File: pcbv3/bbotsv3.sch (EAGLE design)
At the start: 24 parts

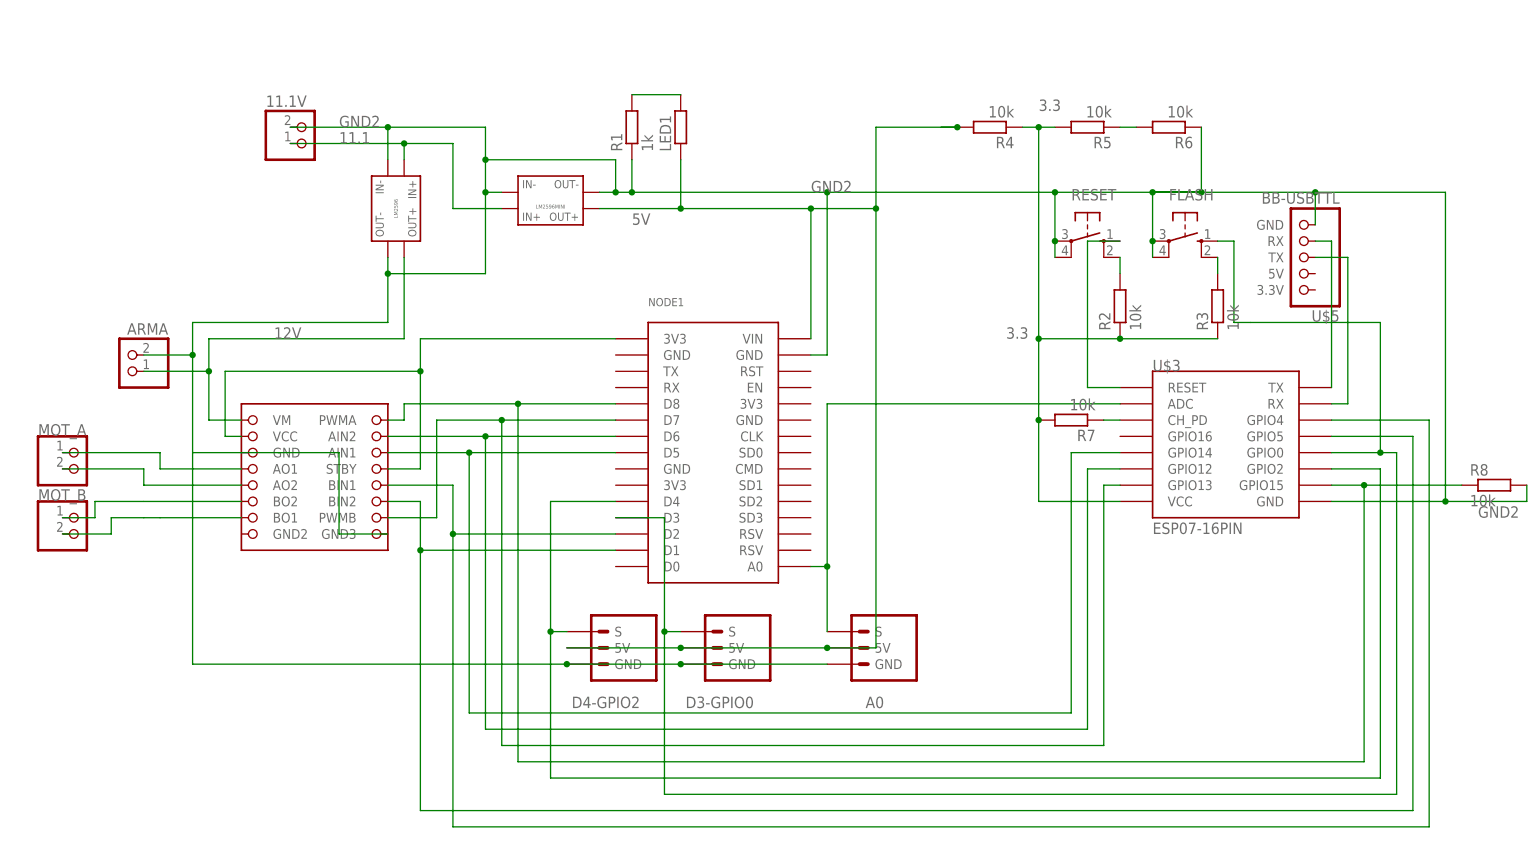
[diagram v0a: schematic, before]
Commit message: changed version of lm2596mini
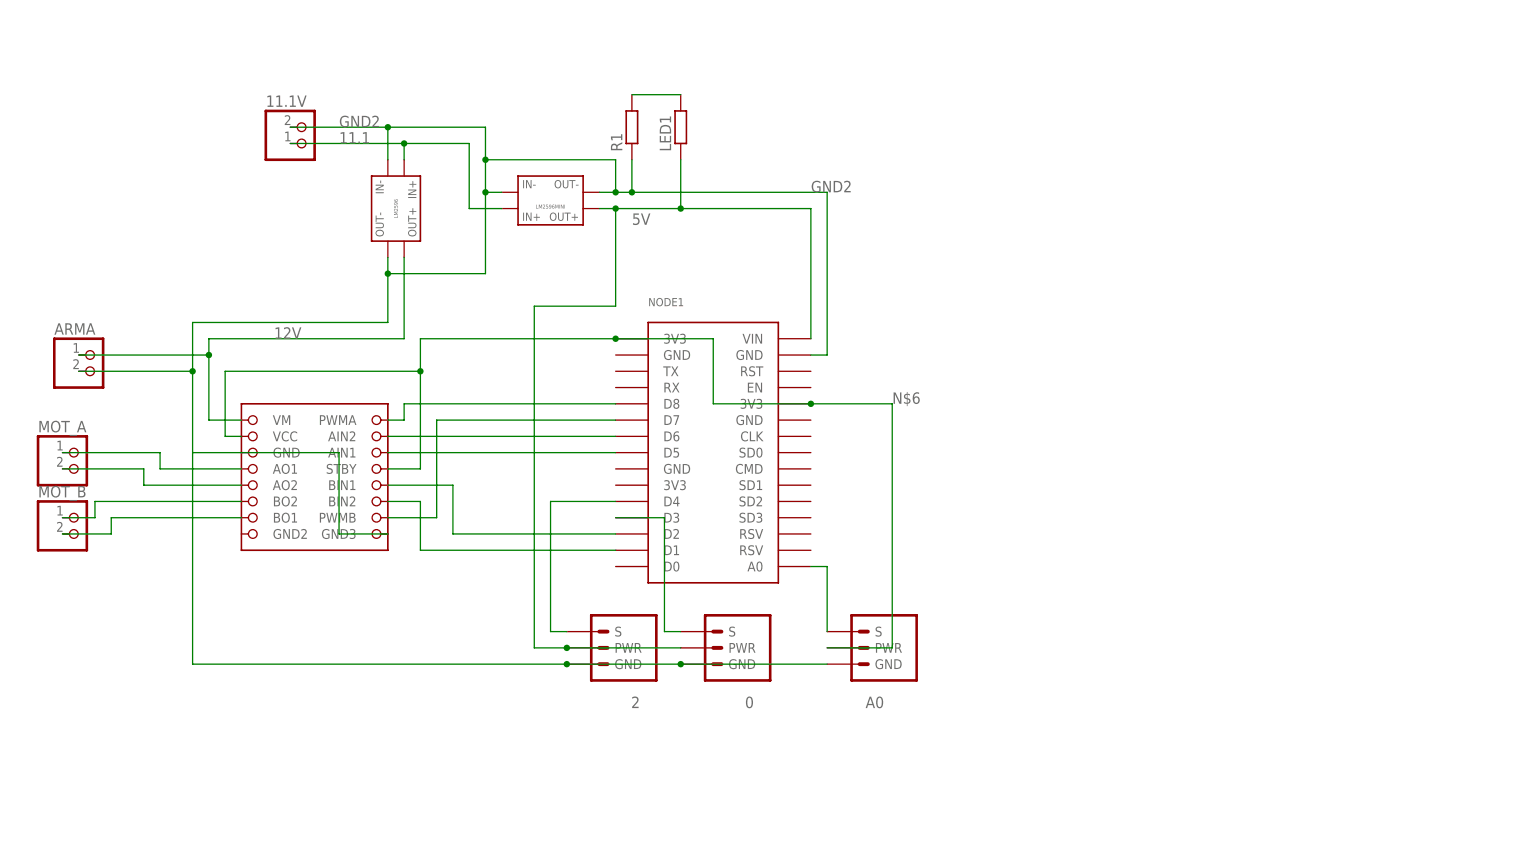
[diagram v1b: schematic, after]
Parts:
- removed D3-GPIO0, D4-GPIO2: BB-PIN3, my-library:BB-PIN3
- removed FLASH, RESET: (no value), switch-omron:10-XX
- removed R2, R3, R4, R5, R6, R7, R8: 10k, my-library:BB-RESM0805
- removed U$4: BB-LM2596MINI, my-library:BB-LM2596MINI
- removed U$5: BB-USBTTL, my-library:BB-USBTTL
- added 0, 2: BB-PIN3BB-PIN3, my-library:BB-PIN3BB-PIN3
- A0: value BB-PIN3 -> 3.3; device my-library:BB-PIN3 -> my-library:BB-PIN3BB-PIN3
- ARMA, MOT_A, MOT_B: device adafruit:JST_2PIN-THM -> my-library:JST_2PIN
- LED1: device my-library:BB-RESM0805 -> my-library:BB-R0805
- R1: value 1k -> BB-R1205; device my-library:BB-RESM0805 -> my-library:BB-R1205
- U$3: value ESP07-16PIN -> BB-LM2596MINILM2596MINIV2; device esp8266modules:ESP07-16PIN -> my-library:BB-LM2596MINILM2596MINIV2
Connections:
- removed net 3.3: R2.1, R3.1, R4.1, R5.2, R7.2, U$3.VCC
- removed net N$17: NODE1.3V3@1, U$2.STBY, U$2.VCC
- removed net N$19: U$3.TX, U$5.RX
- removed net N$20: U$3.RX, U$5.TX
- removed net N$22: R2.2, RESET.S1
- removed net N$23: FLASH.S1, R3.2
- removed net N$25: R5.1, R6.2
- removed net N$27: RESET.S, U$3.RESET
- removed net N$28: R7.1, U$3.CH_PD
- new net N$6: A0.PWR, NODE1.3V3@1, NODE1.3V3@3, U$2.STBY, U$2.VCC
- net 11.1: now also U$3.IN+; no longer U$4.IN+
- net 12V: now also ARMA.1; no longer ARMA.2
- net 5V: now also 0.PWR, 2.PWR, U$3.OUT+; no longer A0.5V, D3-GPIO0.5V, D4-GPIO2.5V, R4.2, U$4.OUT+
- net GND2: now also 0.GND, 2.GND, ARMA.2, U$3.IN-, U$3.OUT-; no longer ARMA.1, D3-GPIO0.GND, D4-GPIO2.GND, FLASH.P, FLASH.P1, R6.1, R8.2, RESET.P, RESET.P1, U$3.GND, U$4.IN-, U$4.OUT-, U$5.GND
- net N$10: no longer U$3.GPIO5
- net N$12: now also 2.S; no longer D4-GPIO2.S, U$3.GPIO2
- net N$13: now also MOT_A.2; no longer MOT_A.1
- net N$14: now also MOT_A.1; no longer MOT_A.2
- net N$15: now also MOT_B.1; no longer MOT_B.2
- net N$16: now also MOT_B.2; no longer MOT_B.1
- net N$18: now also 0.S; no longer D3-GPIO0.S, FLASH.S, U$3.GPIO0
- net N$21: no longer U$3.ADC
- net N$4: no longer R8.1, U$3.GPIO15
- net N$5: no longer U$3.GPIO13
- net N$7: no longer U$3.GPIO12
- net N$8: no longer U$3.GPIO14
- net N$9: no longer U$3.GPIO4
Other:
- moved on the sheet: ARMA, MOT_A, MOT_B

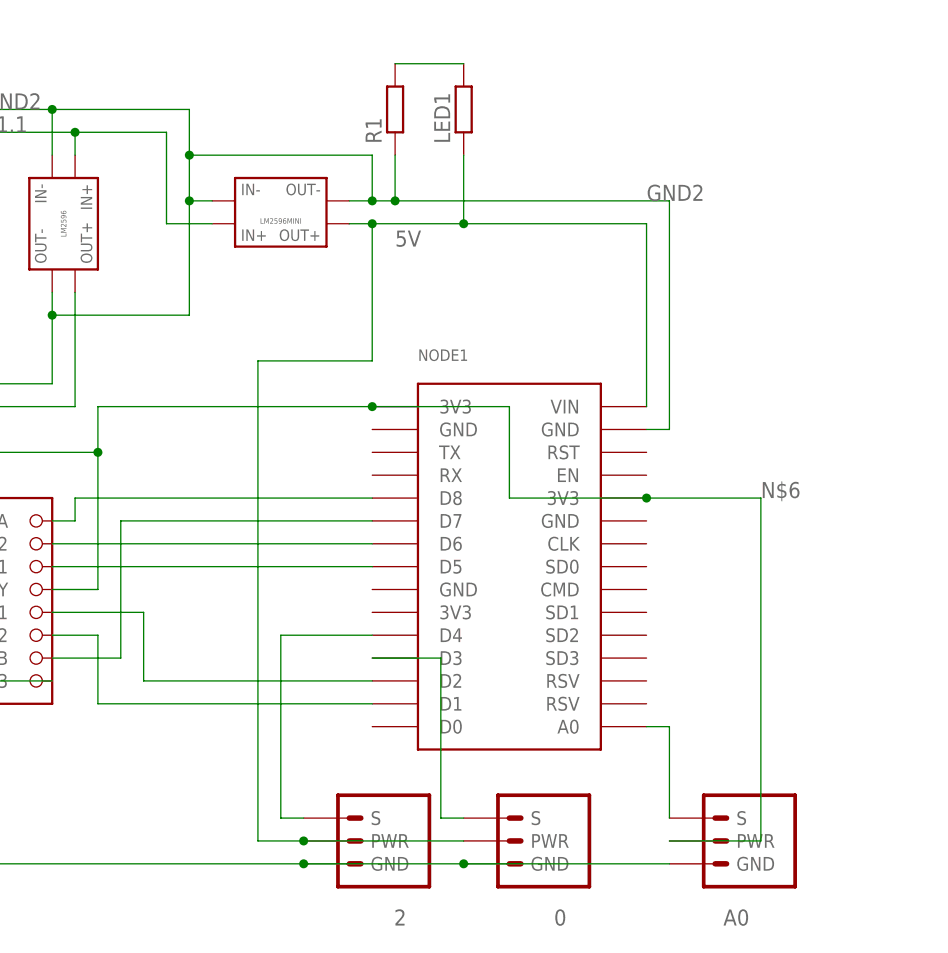
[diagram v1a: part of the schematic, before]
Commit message: added connections for voltage tester
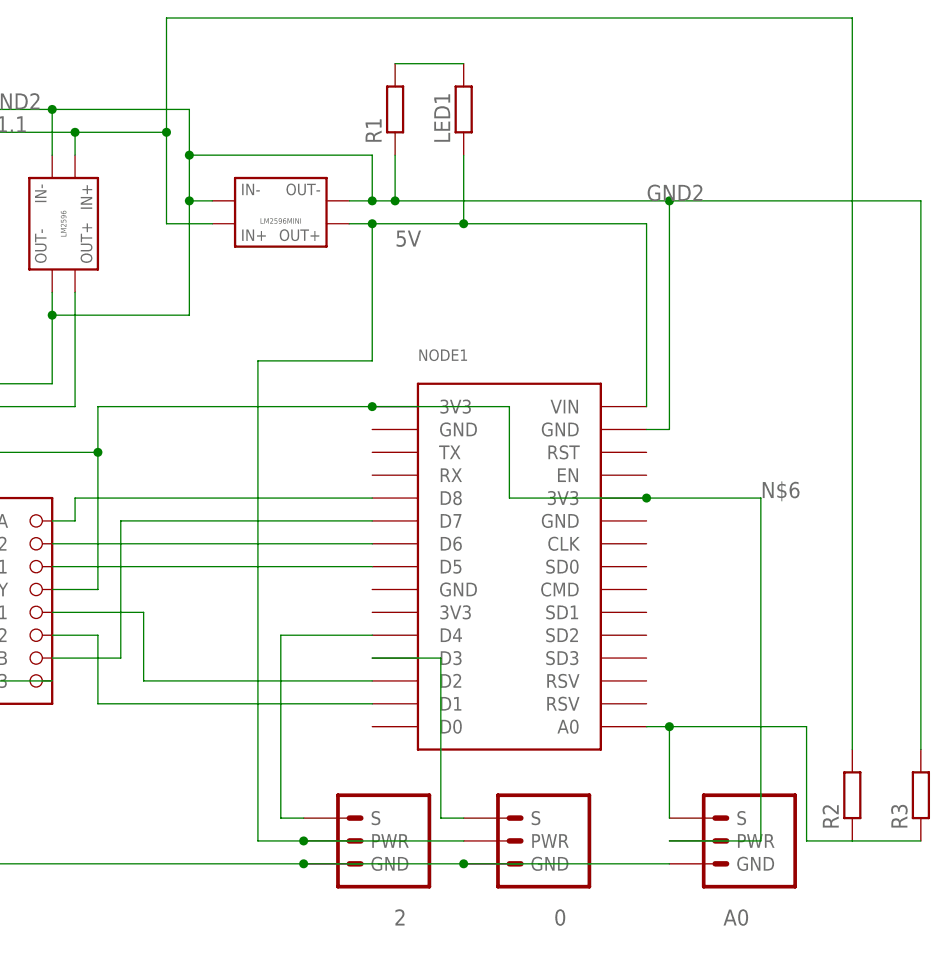
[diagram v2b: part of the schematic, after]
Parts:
- added R2, R3: BB-R1205, my-library:BB-R1205
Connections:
- removed net N$21: A0.S, NODE1.A0
- new net N$1: A0.S, NODE1.A0, R2.1, R3.1
- net 11.1: now also R2.2
- net GND2: now also R3.2
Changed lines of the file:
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@@
 <part name="MOT_B" library="my-library" library_urn="urn:adsk.eagle:library:37248401" deviceset="JST_2PIN" device="" package3d_urn="urn:adsk.eagle:package:39750906/1"/>
 <part name="U$3" library="my-library" library_urn="urn:adsk.eagle:library:37248401" deviceset="BB-LM2596MINI" device="LM2596MINIV2" package3d_urn="urn:adsk.eagle:package:39782154/1"/>
+<part name="R2" library="my-library" library_urn="urn:adsk.eagle:library:37248401" deviceset="BB-R1205" device="" package3d_urn="urn:adsk.eagle:package:39750174/1"/>
+<part name="R3" library="my-library" library_urn="urn:adsk.eagle:library:37248401" deviceset="BB-R1205" device="" package3d_urn="urn:adsk.eagle:package:39750174/1"/>
 </parts>
 <sheets>
@@
 </instance>
 <instance part="U$3" gate="G$1" x="-2.54" y="101.6" smashed="yes"/>
+<instance part="R2" gate="G$1" x="60.96" y="38.1" smashed="yes" rot="R90">
+<attribute name="NAME" x="59.4614" y="34.29" size="1.778" layer="95" rot="R90"/>
+</instance>
+<instance part="R3" gate="G$1" x="68.58" y="38.1" smashed="yes" rot="R90">
+<attribute name="NAME" x="67.0814" y="34.29" size="1.778" layer="95" rot="R90"/>
+</instance>
 </instances>
 <busses>
@@
 <wire x1="-15.24" y1="101.6" x2="-10.16" y2="101.6" width="0.1524" layer="91"/>
 <pinref part="U$3" gate="G$1" pin="IN+"/>
+<wire x1="-15.24" y1="111.76" x2="-15.24" y2="124.46" width="0.1524" layer="91"/>
+<junction x="-15.24" y="111.76"/>
+<pinref part="R2" gate="G$1" pin="2"/>
+<wire x1="-15.24" y1="124.46" x2="60.96" y2="124.46" width="0.1524" layer="91"/>
+<wire x1="60.96" y1="124.46" x2="60.96" y2="43.18" width="0.1524" layer="91"/>
 </segment>
 </net>
@@
 <pinref part="U$3" gate="G$1" pin="IN-"/>
 <pinref part="U$3" gate="G$1" pin="OUT-"/>
+<pinref part="R3" gate="G$1" pin="2"/>
+<wire x1="68.58" y1="43.18" x2="68.58" y2="104.14" width="0.1524" layer="91"/>
+<wire x1="68.58" y1="104.14" x2="40.64" y2="104.14" width="0.1524" layer="91"/>
+<junction x="40.64" y="104.14"/>
 </segment>
 </net>
@@
 <wire x1="-63.5" y1="63.5" x2="-78.74" y2="63.5" width="0.1524" layer="91"/>
 <pinref part="MOT_A" gate="G$1" pin="1"/>
-</segment>
-</net>
-<net name="N$21" class="0">
-<segment>
-<pinref part="NODE1" gate="G$1" pin="A0"/>
-<wire x1="40.64" y1="45.72" x2="38.1" y2="45.72" width="0.1524" layer="91"/>
-<pinref part="A0" gate="G$1" pin="S"/>
-<wire x1="40.64" y1="45.72" x2="40.64" y2="35.56" width="0.1524" layer="91"/>
 </segment>
 </net>
@@
 </segment>
 </net>
+<net name="N$1" class="0">
+<segment>
+<pinref part="R2" gate="G$1" pin="1"/>
+<pinref part="R3" gate="G$1" pin="1"/>
+<wire x1="60.96" y1="33.02" x2="68.58" y2="33.02" width="0.1524" layer="91"/>
+<wire x1="60.96" y1="33.02" x2="55.88" y2="33.02" width="0.1524" layer="91"/>
+<wire x1="55.88" y1="33.02" x2="55.88" y2="45.72" width="0.1524" layer="91"/>
+<pinref part="NODE1" gate="G$1" pin="A0"/>
+<wire x1="40.64" y1="45.72" x2="38.1" y2="45.72" width="0.1524" layer="91"/>
+<pinref part="A0" gate="G$1" pin="S"/>
+<wire x1="40.64" y1="45.72" x2="40.64" y2="35.56" width="0.1524" layer="91"/>
+<wire x1="55.88" y1="45.72" x2="40.64" y2="45.72" width="0.1524" layer="91"/>
+<junction x="40.64" y="45.72"/>
+</segment>
+</net>

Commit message: finish pcb, waiting review
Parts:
- removed 11.1V: (no value), adafruit:JST_2PIN-THM
- removed A0: 3.3, my-library:BB-PIN3BB-PIN3
- removed MOT_A, MOT_B: (no value), my-library:JST_2PIN
- added ARMA1, ARMA2, ARMA3: TERMINAL_2P, KF301-2P-Terminal:TERMINAL_2P
- added D1: (no value), adafruit:DIODEDO-1N4148
- added E1: MSTBA2, con-phoenix-508:MSTBA2
- added Q1, Q2: (no value), adafruit:MOSFET-NWAVE
- added R4, R5, R6, R7: 10k, my-library:BB-R1205
- ARMA: value (none) -> TERMINAL_2P; device my-library:JST_2PIN -> KF301-2P-Terminal:TERMINAL_2P
- R1: value BB-R1205 -> 100
- R2: value BB-R1205 -> 10k
- R3: value BB-R1205 -> 1k
- renumbered LED1 to 5VREG
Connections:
- removed net N$16: MOT_B.2, U$2.BO1
- new net 3V3: NODE1.3V3@1, NODE1.3V3@2, NODE1.3V3@3, Q1.G, Q2.G, R4.2, R5.2, U$2.STBY, U$2.VCC
- new net N$11: 2.S, Q1.D, R6.1
- new net N$19: NODE1.D4, Q1.S, R5.1
- new net N$2: ARMA3.1, D1.A, E1-1.1
- net 11.1: now also D1.C; no longer 11.1V.2
- net 5V: now also R6.2, R7.2
- net GND2: now also ARMA3.2, E1-2.1, NODE1.GND@1, NODE1.GND@2, NODE1.GND@3, U$2.GND2; no longer 11.1V.1, A0.GND
- net N$1: no longer A0.S
- net N$12: now also NODE1.D3, Q2.S, R4.1; no longer 2.S, NODE1.D4
- net N$13: now also ARMA1.2; no longer MOT_A.2
- net N$14: now also ARMA1.1; no longer MOT_A.1
- net N$15: now also ARMA2.2, U$2.BO1; no longer MOT_B.1, U$2.BO2
- net N$18: now also Q2.D, R7.1; no longer NODE1.D3
- net N$6: now also ARMA2.1, U$2.BO2; no longer A0.PWR, NODE1.3V3@1, NODE1.3V3@3, U$2.STBY, U$2.VCC
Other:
- moved on the sheet: 0, 2, R2, R3

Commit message: ready to manufacture, review done
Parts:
- D1: device adafruit:DIODEDO-1N4148 -> my-library:DIODEDO-1N4148
- renumbered E1 to BAT1
